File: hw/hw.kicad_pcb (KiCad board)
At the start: 2 copper layers, 52 x 20 mm, 41 parts, among them CN1 PJ-320D, U1 ICE40LP1K-QN84, U2 MAX98357AETE+T, U3 AP2112K-3.3, U4 AP2112K-1.8, U5 MIC5219-2.8YM5, U6 AT25SF081-SSHD-X, U7 YF4016M00033T8188092, U8 PM004MNIATR

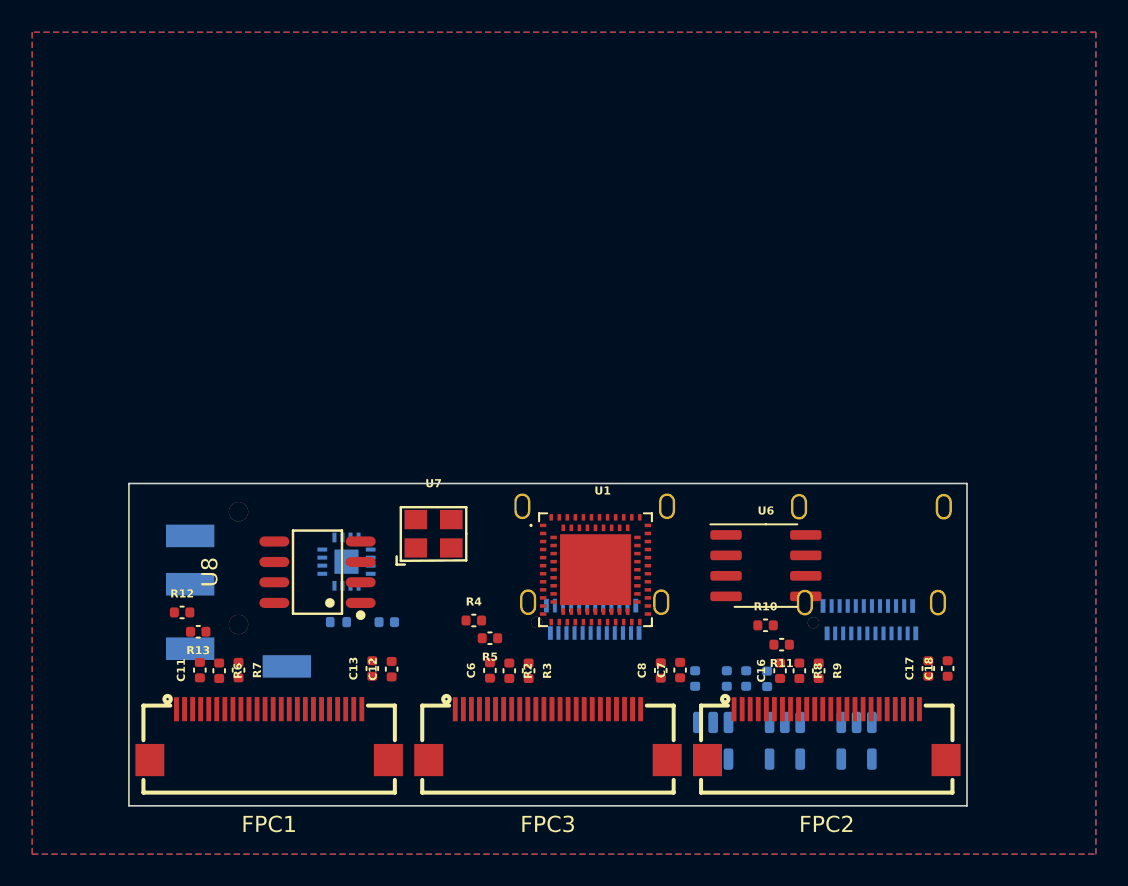
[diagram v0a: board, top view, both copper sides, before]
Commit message: switch to a fpga with more gpio + doc
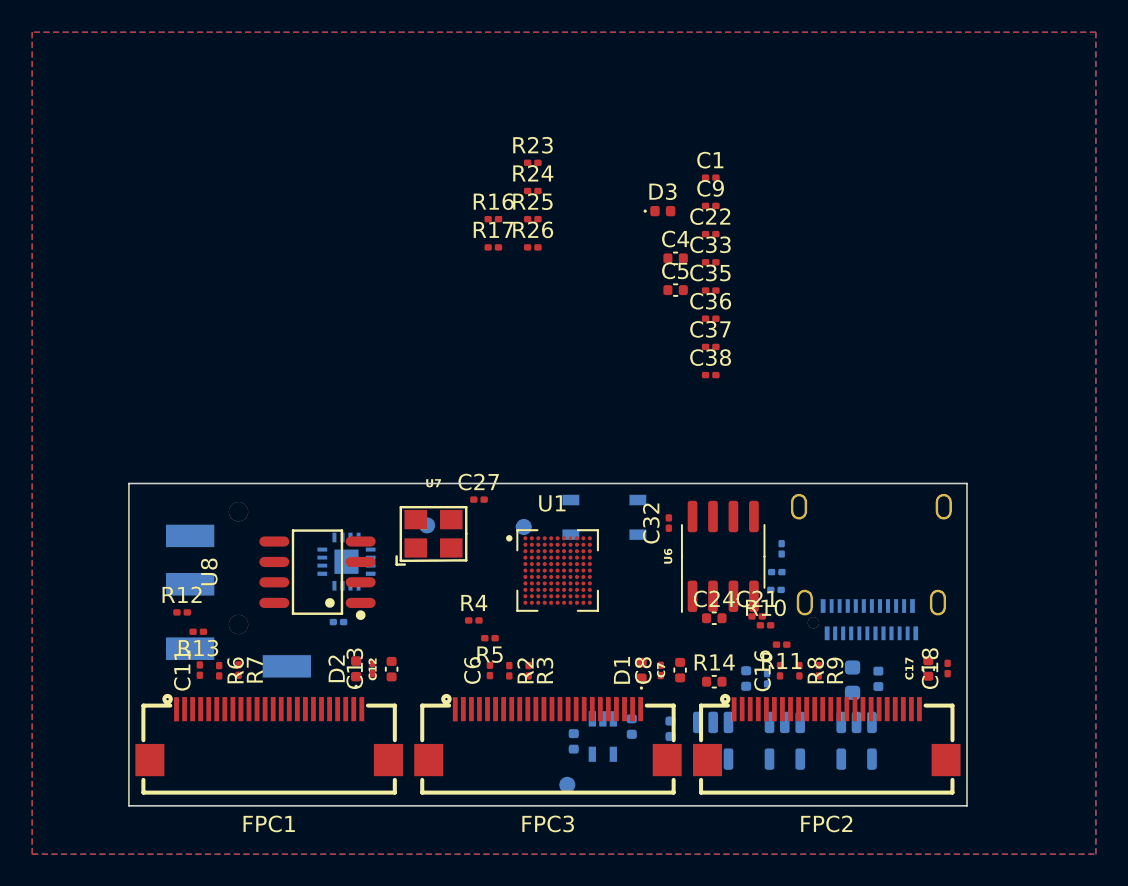
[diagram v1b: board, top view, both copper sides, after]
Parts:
- removed USB2: 12401832E402A, easyeda2kicad:USB-C-TH_12401832E402A
- added C21: 100nF, Capacitor_SMD:C_0201_0603Metric, F.Cu at (145.0, 80.2)
- added C22: 100nF, Capacitor_SMD:C_0201_0603Metric, F.Cu at (142.1, 56.5)
- added C24: 10uF, Capacitor_SMD:C_0402_1005Metric, F.Cu at (142.3, 80.4)
- added C26: 1uF, Capacitor_SMD:C_0402_1005Metric, B.Cu at (137.2, 87.1)
- added C27: 100nF, Capacitor_SMD:C_0201_0603Metric, F.Cu at (127.7, 73.0)
- added C31: 1uF, Capacitor_SMD:C_0402_1005Metric, B.Cu at (133.6, 88.0)
- added C32: 100nF, Capacitor_SMD:C_0201_0603Metric, F.Cu at (139.5, 74.5)
- added C33: 10nF, Capacitor_SMD:C_0201_0603Metric, F.Cu at (142.1, 58.3)
- added C34: 10uF, Capacitor_SMD:C_0402_1005Metric, B.Cu at (152.5, 84.1)
- added C35: 10nF, Capacitor_SMD:C_0201_0603Metric, F.Cu at (142.1, 60.0)
- added C36: 10nF, Capacitor_SMD:C_0201_0603Metric, F.Cu at (142.1, 61.8)
- added C37: 10nF, Capacitor_SMD:C_0201_0603Metric, F.Cu at (142.1, 63.5)
- added C38: 100nF, Capacitor_SMD:C_0201_0603Metric, F.Cu at (142.1, 65.3)
- added C4: 22uF, Capacitor_SMD:C_0402_1005Metric, F.Cu at (139.9, 58.0)
- added C5: 22uF, Capacitor_SMD:C_0402_1005Metric, F.Cu at (139.9, 60.0)
- added C9: 100nF, Capacitor_SMD:C_0201_0603Metric, F.Cu at (142.1, 54.8)
- added D1: D, Diode_SMD:D_0402_1005Metric, F.Cu at (137.8, 83.6)
- added D2: D, Diode_SMD:D_0402_1005Metric, F.Cu at (120.1, 83.5)
- added D3: D, Diode_SMD:D_0402_1005Metric, F.Cu at (139.1, 55.1)
- added L2: Bead, Inductor_SMD:L_0603_1608Metric, B.Cu at (150.9, 84.2)
- added R14: 0R, Capacitor_SMD:C_0402_1005Metric, F.Cu at (142.3, 84.3)
- added R16: 5.1K, Resistor_SMD:R_0201_0603Metric, F.Cu at (128.6, 55.6)
- added R17: 100, Resistor_SMD:R_0201_0603Metric, F.Cu at (128.6, 57.4)
- added R18: 1.5k, Resistor_SMD:R_0201_0603Metric, B.Cu at (146.5, 76.1)
- added R19: 68, Resistor_SMD:R_0201_0603Metric, B.Cu at (146.2, 77.5)
- added R20: 68, Resistor_SMD:R_0201_0603Metric, B.Cu at (146.1, 78.6)
- added R23: 10k, Resistor_SMD:R_0201_0603Metric, F.Cu at (131.1, 52.1)
- added R24: 10k, Resistor_SMD:R_0201_0603Metric, F.Cu at (131.1, 53.9)
- added R25: R, Resistor_SMD:R_0201_0603Metric, F.Cu at (131.1, 55.6)
- added R26: 10k, Resistor_SMD:R_0201_0603Metric, F.Cu at (131.1, 57.4)
- added SW1: SW_Push, tinyfpga:PTS_810_SMT_Switch, B.Cu at (135.5, 74.1)
- added TP1: TEST, TestPoint:TestPoint_Pad_D1.0mm, B.Cu at (133.2, 90.7)
- added TP2: TEST, TestPoint:TestPoint_Pad_D1.0mm, B.Cu at (124.5, 74.6)
- added TP3: TEST, TestPoint:TestPoint_Pad_D1.0mm, B.Cu at (130.5, 74.7)
- added U10: MIC5365-1.2YC5-TR, tinyfpga:SC-70-C5, B.Cu at (135.4, 87.7)
- C1: value C -> 100nF; footprint Capacitor_SMD:C_0402_1005Metric -> Capacitor_SMD:C_0201_0603Metric; moved to F.Cu
- C11, C13, C14, C16, C18, C6, C8: footprint Capacitor_SMD:C_0402_1005Metric -> Capacitor_SMD:C_0201_0603Metric
- R1: value R -> 5.1K; footprint Resistor_SMD:R_0402_1005Metric -> Resistor_SMD:R_0201_0603Metric
- R10, R11, R12, R13, R2, R3, R4, R5, R6, R7, R8, R9: footprint Capacitor_SMD:C_0402_1005Metric -> Resistor_SMD:R_0201_0603Metric
- U1: value ICE40LP1K-QN84 -> ICE40LP8K-CM121; footprint footprint:LATTICE_ICE40LP1K-QN84 -> footprint:BGA121N40P11X11_500X500X100N
- moved C1 34.1 mm to (142.1, 53.0), turned to 0 degrees
- moved C3 6.27 mm to (139.6, 89.3), turned to 90 degrees
- moved C2 3.47 mm to (139.6, 87.2)
- moved U6 2.71 mm to (142.9, 76.5), turned to 90 degrees
- moved U1 2.35 mm to (132.6, 77.4)
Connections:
- C1 pad 1: unconnected-(C1-Pad1) -> +3.3V
- C1 pad 2: unconnected-(C1-Pad2) -> GND
- R1 pad 1: unconnected-(R1-Pad1) -> Net-(USB1-CC2)
- R1 pad 2: unconnected-(R1-Pad2) -> GND
- U1 pad A1: /DVP2_SDA -> /DVP0_Y8
- U1 pad A10: /DVP2_Y5 -> unconnected-(U1A-IOT_170-PadA10)
- U1 pad A11: /DVP2_Y3 -> unconnected-(U1A-IOT_168-PadA11)
- U1 pad A2: /DVP1_SDA -> /DVP2_Y2
- U1 pad A3: /DVP0_SDA -> /DVP0_MCLK
- U1 pad A4: /DVP2_VSYNC -> USB_P
- U1 pad A5: /DVP2_Y8 -> /DVP1_VSYNC
- U1 pad A6: Net-(U1-GND-PadA18) -> /DVP2_PCLK
- U1 pad A7: +1V2 -> /DVP2_Y4
- U1 pad A8: unconnected-(U1-IOL_6B_GBIN7-PadA8) -> /DVP1_Y9
- U1 pad A9: unconnected-(U1-IOL_7A_GBIN6-PadA9) -> USB_PU
- U1 pad B1: /DVP2_SCL -> GND
- U1 pad B10: /DVP1_VSYNC -> VPP_FAST
- U1 pad B11: /DVP1_HREF -> /DVP2_MCLK
- U1 pad B2: /DVP1_SCL -> CLK
- U1 pad B3: /DVP0_SCL -> /DVP2_Y3
- U1 pad B4: /DVP2_Y9 -> /DVP1_Y8
- U1 pad B5: /DVP2_Y7 -> USB_N
- U1 pad B6: +3.3V -> unconnected-(U1A-IOT_198_GBIN0-PadB6)
- U1 pad B7: /DVP2_Y6 -> unconnected-(U1A-IOT_197_GBIN1-PadB7)
- U1 pad B8: /DVP2_Y4 -> +3V3
- U1 pad B9: /DVP2_Y2 -> GND
- U4 pad 1: unconnected-(U4-VIN-Pad1) -> VBUS
- U4 pad 3: unconnected-(U4-EN-Pad3) -> VBUS
- U5 pad 1: unconnected-(U5-IN-Pad1) -> VBUS
- U5 pad 3: unconnected-(U5-EN-Pad3) -> VBUS
- U6 pad 1: unconnected-(U6-~{CS}-Pad1) -> SS
- U6 pad 2: unconnected-(U6-SO/IO1-Pad2) -> SDI
- U6 pad 3: unconnected-(U6-~{WP}/IO2-Pad3) -> 82
- U6 pad 5: unconnected-(U6-SI/IO0-Pad5) -> SDO
- U6 pad 6: unconnected-(U6-SCK-Pad6) -> SCK
- U6 pad 7: unconnected-(U6-~{HOLD}/IO3-Pad7) -> 109
- U6 pad 8: unconnected-(U6-VCC-Pad8) -> +3.3V
- U7 pad 1: unconnected-(U7-Tri-state-Pad1) -> Net-(U7-Tri-state)
- U7 pad 3: unconnected-(U7-Output-Pad3) -> CLK
- U7 pad 4: unconnected-(U7-Vdd-Pad4) -> +3V3
- USB1 pad 0: unconnected-(USB1-Pad0) -> GND
- USB1 pad A4: unconnected-(USB1-VBUS-PadA4) -> VBUS
- USB1 pad A5: unconnected-(USB1-CC1-PadA5) -> Net-(USB1-CC1)
- USB1 pad A6: unconnected-(USB1-D+-PadA6) -> /USB_D_P
- USB1 pad A7: unconnected-(USB1-D--PadA7) -> /USB_D_N
- USB1 pad A9: unconnected-(USB1-VBUS-PadA9) -> VBUS
- USB1 pad B4: unconnected-(USB1-VBUS-PadB4) -> VBUS
- USB1 pad B5: unconnected-(USB1-CC2-PadB5) -> Net-(USB1-CC2)
- USB1 pad B6: unconnected-(USB1-D+-PadB6) -> /USB_D_P
- USB1 pad B7: unconnected-(USB1-D--PadB7) -> /USB_D_N
- USB1 pad B9: unconnected-(USB1-VBUS-PadB9) -> VBUS
